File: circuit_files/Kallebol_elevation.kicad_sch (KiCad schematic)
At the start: 56 parts, among them IC1 BD62130AEFJ-E2, J1 Home_switch, J10 Conn_01x05_Male, J11 UART/I2C, J2 Encoder, J3 Limit Switch, J4 Power in, J5 power_out, J6 Screw_Terminal_01x02, J7 Screw_Terminal_01x02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

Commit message: layout done
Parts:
- removed JP2: Jumper_3, Connector_PinSocket_2.54mm:PinSocket_1x03_P2.54mm_Vertical, symbol Jumper:Jumper_3_Bridged12
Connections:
- net +12V: now also J8.10 (Pin_10)
- net +5V: now also J10.5 (Pin_5); no longer J8.10 (Pin_10)
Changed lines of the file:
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@@
-    )
-  )
-  (symbol (lib_id "power:+3V3") (at 241.935 79.375 0) (unit 1)
-    (in_bom yes) (on_board yes) (dnp no) (fields_autoplaced)
-    (property "Reference" "#PWR037" (at 241.935 83.185 0)
-      (effects (font (size 1.27 1.27)) hide)
-    )
-    (property "Value" "+3V3" (at 241.935 75.7992 0)
-      (effects (font (size 1.27 1.27)))
-    )
-    (property "Footprint" "" (at 241.935 79.375 0)
-      (effects (font (size 1.27 1.27)) hide)
-    )
-    (property "Datasheet" "" (at 241.935 79.375 0)
-      (effects (font (size 1.27 1.27)) hide)
-    )
-    (pin "1")
-    (instances
-      (project "Kallebol_elevation"
-        (path "/e63e39d7-6ac0-4ffd-8aa3-1841a4541b55"
-          (reference "#PWR037") (unit 1)
-        )
-      )
-      (project "Kallebol_GPIO_fanout"
-        (path "/f263f1e0-afed-421c-96dc-2cc7b196a4ea"
-          (reference "#PWR0124") (unit 1)
-        )
-      )
     )
   )
@@
     )
   )
-  (symbol (lib_id "power:+5V") (at 254.635 79.375 0) (unit 1)
-    (in_bom yes) (on_board yes) (dnp no) (fields_autoplaced)
-    (property "Reference" "#PWR038" (at 254.635 83.185 0)
-      (effects (font (size 1.27 1.27)) hide)
-    )
-    (property "Value" "+5V" (at 254.635 75.7992 0)
-      (effects (font (size 1.27 1.27)))
-    )
-    (property "Footprint" "" (at 254.635 79.375 0)
-      (effects (font (size 1.27 1.27)) hide)
-    )
-    (property "Datasheet" "" (at 254.635 79.375 0)
+  (symbol (lib_id "power:+5V") (at 248.285 83.185 0) (unit 1)
+    (in_bom yes) (on_board yes) (dnp no) (fields_autoplaced)
+    (property "Reference" "#PWR038" (at 248.285 86.995 0)
+      (effects (font (size 1.27 1.27)) hide)
+    )
+    (property "Value" "+5V" (at 248.285 79.6092 0)
+      (effects (font (size 1.27 1.27)))
+    )
+    (property "Footprint" "" (at 248.285 83.185 0)
+      (effects (font (size 1.27 1.27)) hide)
+    )
+    (property "Datasheet" "" (at 248.285 83.185 0)
       (effects (font (size 1.27 1.27)) hide)
     )
@@
     )
   )
-  (symbol (lib_id "power:+5V") (at 110.49 109.22 0) (unit 1)
-    (in_bom yes) (on_board yes) (dnp no) (fields_autoplaced)
+  (symbol (lib_id "power:GND") (at 145.415 124.46 0) (unit 1)
+    (in_bom yes) (on_board yes) (dnp no)
+    (property "Reference" "#PWR0106" (at 145.415 130.81 0)
+      (effects (font (size 1.27 1.27)) hide)
+    )
+    (property "Value" "GND" (at 145.542 128.8542 0)
+      (effects (font (size 1.27 1.27)))
+    )
+    (property "Footprint" "" (at 145.415 124.46 0)
+      (effects (font (size 1.27 1.27)) hide)
+    )
+    (property "Datasheet" "" (at 145.415 124.46 0)
+      (effects (font (size 1.27 1.27)) hide)
+    )
+    (pin "1")
+    (instances
+      (project "Kallebol_elevation"
+        (path "/e63e39d7-6ac0-4ffd-8aa3-1841a4541b55"
+          (reference "#PWR0106") (unit 1)
+        )
+      )
+    )
+  )
+  (symbol (lib_id "power:+12V") (at 110.49 109.22 0) (unit 1)
+    (in_bom yes) (on_board yes) (dnp no)
     (property "Reference" "#PWR034" (at 110.49 113.03 0)
       (effects (font (size 1.27 1.27)) hide)
     )
-    (property "Value" "+5V" (at 110.49 105.6442 0)
+    (property "Value" "+12V" (at 110.871 104.8258 0)
       (effects (font (size 1.27 1.27)))
     )
@@
         (path "/e63e39d7-6ac0-4ffd-8aa3-1841a4541b55"
           (reference "#PWR034") (unit 1)
-        )
-      )
-      (project "Kallebol_GPIO_fanout"
-        (path "/f263f1e0-afed-421c-96dc-2cc7b196a4ea"
-          (reference "#PWR0111") (unit 1)
-        )
-      )
-    )
-  )
-  (symbol (lib_id "power:GND") (at 145.415 124.46 0) (unit 1)
-    (in_bom yes) (on_board yes) (dnp no)
-    (property "Reference" "#PWR0106" (at 145.415 130.81 0)
-      (effects (font (size 1.27 1.27)) hide)
-    )
-    (property "Value" "GND" (at 145.542 128.8542 0)
-      (effects (font (size 1.27 1.27)))
-    )
-    (property "Footprint" "" (at 145.415 124.46 0)
-      (effects (font (size 1.27 1.27)) hide)
-    )
-    (property "Datasheet" "" (at 145.415 124.46 0)
-      (effects (font (size 1.27 1.27)) hide)
-    )
-    (pin "1")
-    (instances
-      (project "Kallebol_elevation"
-        (path "/e63e39d7-6ac0-4ffd-8aa3-1841a4541b55"
-          (reference "#PWR0106") (unit 1)
         )
       )
@@
         )
       )
-    )
-  )
-  (symbol (lib_id "Jumper:Jumper_3_Bridged12") (at 248.285 79.375 0) (unit 1)
-    (in_bom yes) (on_board yes) (dnp no) (fields_autoplaced)
-    (property "Reference" "JP2" (at 248.285 75.5009 0)
-      (effects (font (size 1.27 1.27)))
-    )
-    (property "Value" "Jumper_3" (at 248.285 77.4219 0)
-      (effects (font (size 1.27 1.27)))
-    )
-    (property "Footprint" "Connector_PinSocket_2.54mm:PinSocket_1x03_P2.54mm_Vertical" (at 248.285 79.375 0)
-      (effects (font (size 1.27 1.27)) hide)
-    )
-    (property "Datasheet" "~" (at 248.285 79.375 0)
-      (effects (font (size 1.27 1.27)) hide)
-    )
-    (pin "1")
-    (pin "2")
-    (pin "3")
-    (instances
-      (project "Kallebol_elevation"
-        (path "/e63e39d7-6ac0-4ffd-8aa3-1841a4541b55"
-          (reference "JP2") (unit 1)
-        )
-      )
-      (project "Kallebol_GPIO_fanout"
-        (path "/f263f1e0-afed-421c-96dc-2cc7b196a4ea"
-          (reference "JP1") (unit 1)
-        )
-      )

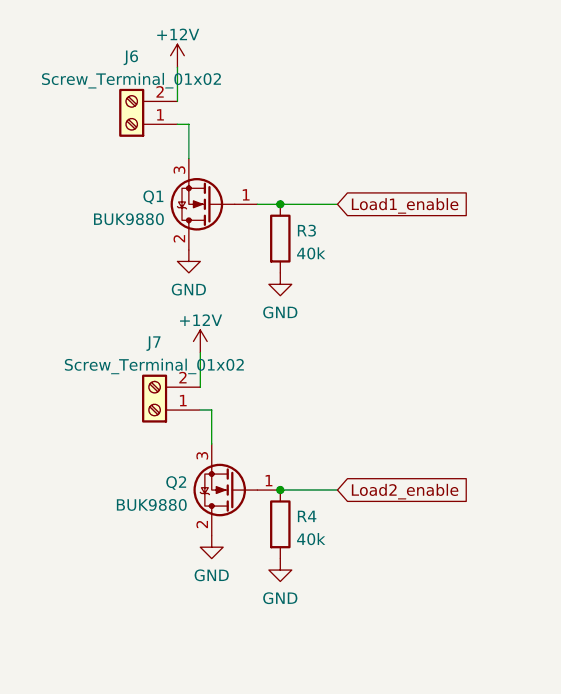
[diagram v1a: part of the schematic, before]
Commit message: fixed issue with reversed mosfet
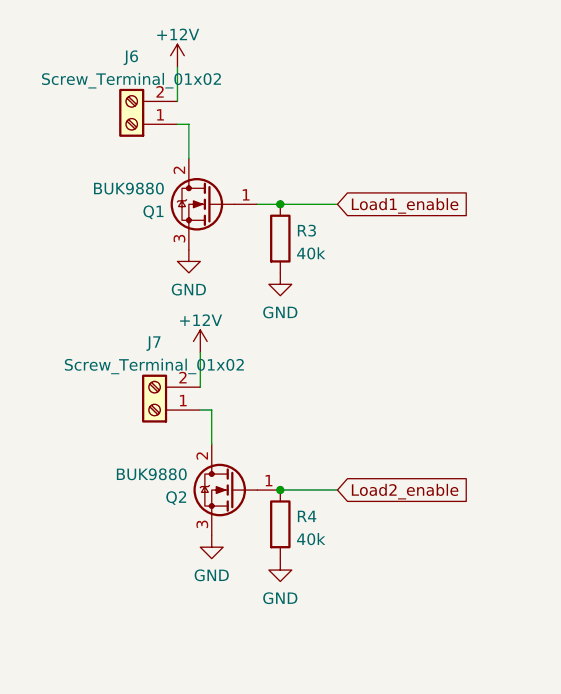
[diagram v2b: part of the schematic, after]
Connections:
- net GND: now also Q1.3 (S), Q2.3 (S); no longer Q1.2 (D), Q2.2 (D)
- net at J7.1 (Pin_1): now also Q2.2 (D); no longer Q2.3 (S)
- net at J6.1 (Pin_1): now also Q1.2 (D); no longer Q1.3 (S)
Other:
- moved on the sheet: Q1, Q2
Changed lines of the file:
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@@
     )
   )
-  (symbol (lib_id "Device:Q_NMOS_GDS") (at 43.18 127.635 180) (unit 1)
-    (in_bom yes) (on_board yes) (dnp no) (fields_autoplaced)
-    (property "Reference" "Q2" (at 37.973 126.8003 0)
-      (effects (font (size 1.27 1.27)) (justify left))
-    )
-    (property "Value" "BUK9880" (at 37.973 129.3372 0)
-      (effects (font (size 1.27 1.27)) (justify left))
-    )
-    (property "Footprint" "Package_TO_SOT_SMD:SOT-223-3_TabPin2" (at 38.1 130.175 0)
+  (symbol (lib_id "Device:Q_NMOS_GDS") (at 43.18 127.635 0) (mirror y) (unit 1)
+    (in_bom yes) (on_board yes) (dnp no)
+    (property "Reference" "Q2" (at 37.973 128.4697 0)
+      (effects (font (size 1.27 1.27)) (justify left))
+    )
+    (property "Value" "BUK9880" (at 37.973 125.9328 0)
+      (effects (font (size 1.27 1.27)) (justify left))
+    )
+    (property "Footprint" "Package_TO_SOT_SMD:SOT-223-3_TabPin2" (at 38.1 125.095 0)
       (effects (font (size 1.27 1.27)) hide)
     )
@@
     )
   )
-  (symbol (lib_id "Device:Q_NMOS_GDS") (at 40.64 95.885 180) (unit 1)
-    (in_bom yes) (on_board yes) (dnp no) (fields_autoplaced)
-    (property "Reference" "Q1" (at 35.433 95.0503 0)
-      (effects (font (size 1.27 1.27)) (justify left))
-    )
-    (property "Value" "BUK9880" (at 35.433 97.5872 0)
-      (effects (font (size 1.27 1.27)) (justify left))
-    )
-    (property "Footprint" "Package_TO_SOT_SMD:SOT-223-3_TabPin2" (at 35.56 98.425 0)
-      (effects (font (size 1.27 1.27)) hide)
-    )
+  (symbol (lib_id "Device:Q_NMOS_GDS") (at 40.64 95.885 0) (mirror y) (unit 1)
+    (in_bom yes) (on_board yes) (dnp no)
+    (property "Reference" "Q1" (at 35.433 96.7197 0)
+      (effects (font (size 1.27 1.27)) (justify left))
+    )
+    (property "Value" "BUK9880" (at 35.433 94.1828 0)
+      (effects (font (size 1.27 1.27)) (justify left))
+    )
+    (property "Footprint" "Package_TO_SOT_SMD:SOT-223-3_TabPin2" (at 35.56 93.345 0)
+      (effects (font (size 1.27 1.27)) hide)
+    )
